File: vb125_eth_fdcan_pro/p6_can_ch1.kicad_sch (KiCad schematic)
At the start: 32 parts, among them J4 D09P33E4GL00LF, M2 B0505MT-1WR4, Q3 FDN358P, Q4 FDN358P, SW1 DS04-254-2-03BK-SMT, U8 ADM3057E

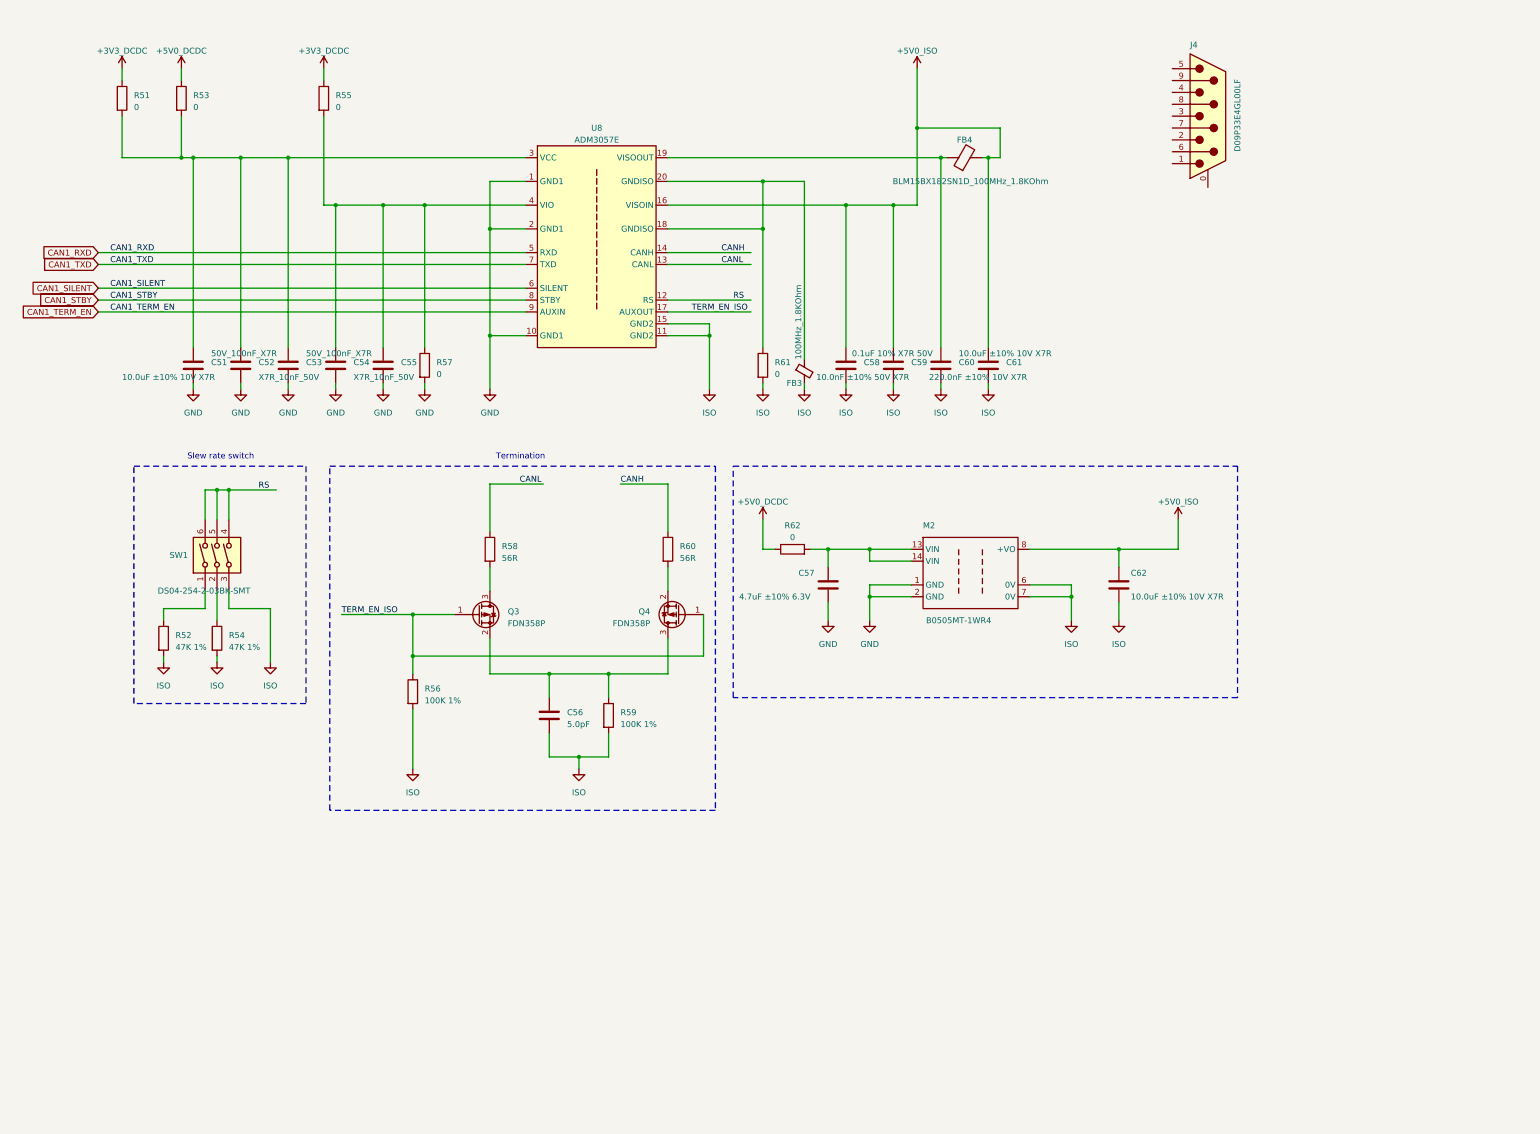
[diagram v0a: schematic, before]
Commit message: CAN schematics. Assign IO on H7.
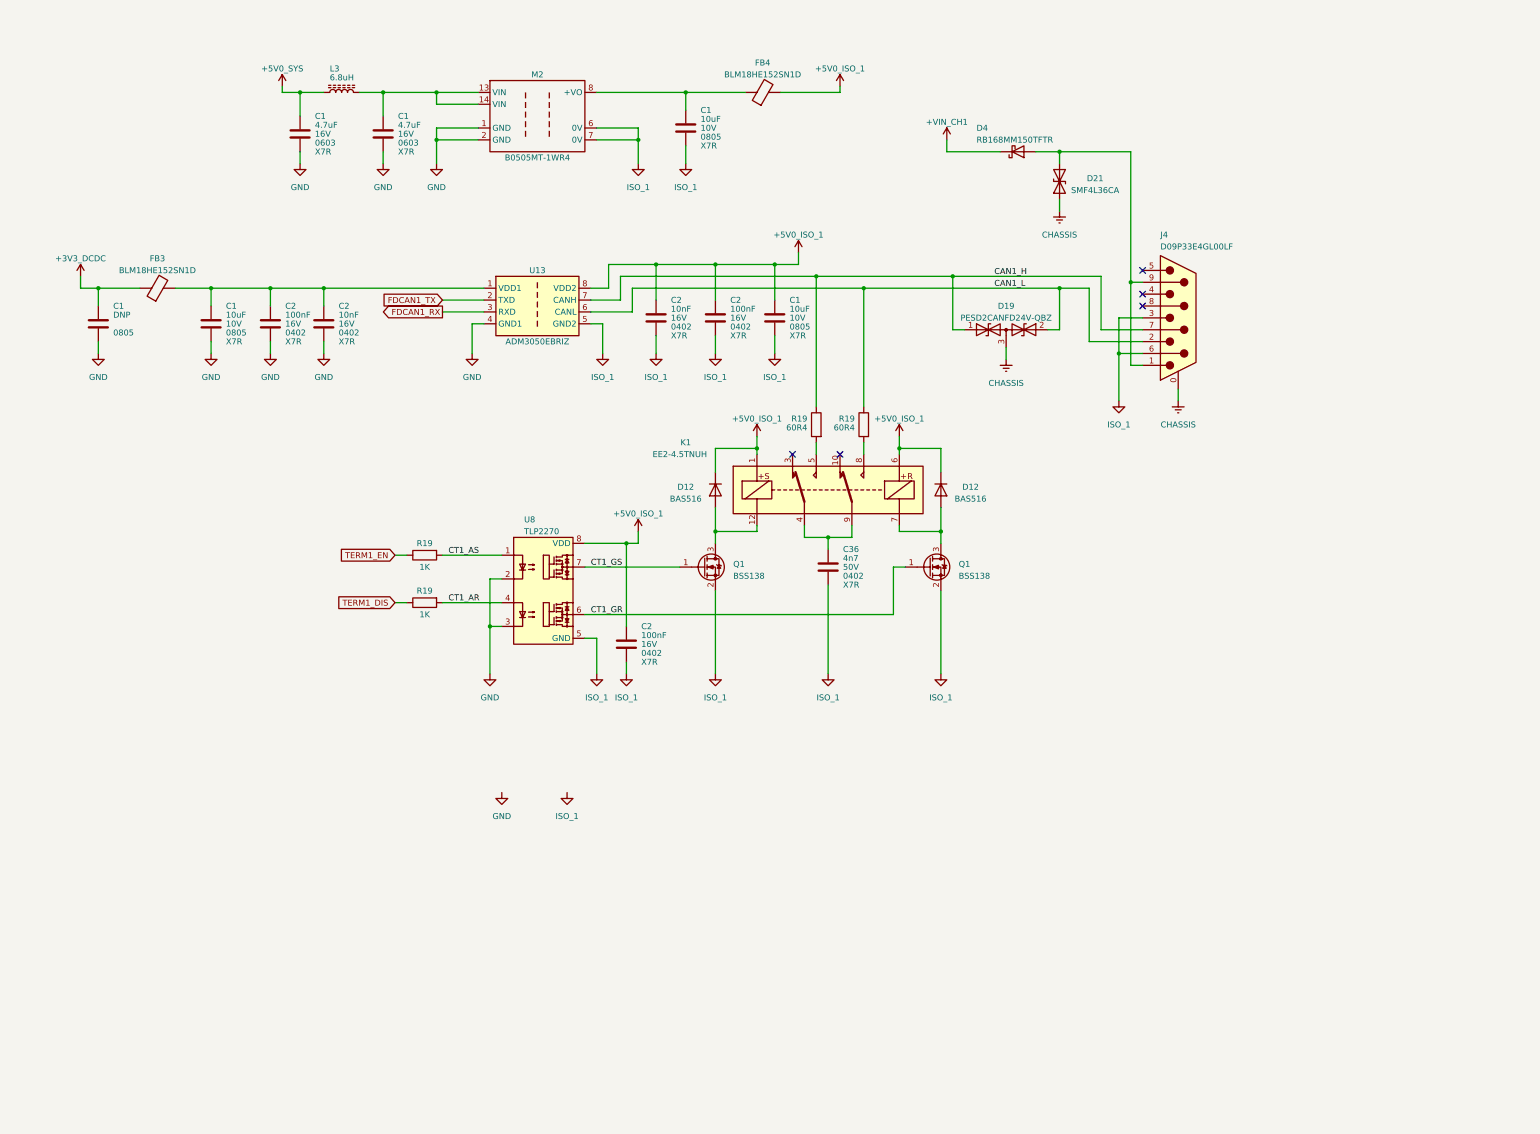
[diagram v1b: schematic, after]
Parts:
- removed C51, C61, C62: 10.0uF ±10% 10V X7R, Capacitor_SMD:C_1206_3216Metric, symbol Device:C
- removed C52, C54: 50V_100nF_X7R, Capacitor_SMD:C_0402_1005Metric, symbol Device:C
- removed C53, C55: X7R_10nF_50V, Capacitor_SMD:C_0402_1005Metric, symbol Device:C
- removed C56: 5.0pF, Capacitor_SMD:C_0402_1005Metric, symbol Device:C
- removed C57: 4.7uF ±10% 6.3V, Capacitor_SMD:C_0603_1608Metric, symbol Device:C
- removed C58: 10.0nF ±10% 50V X7R, Capacitor_SMD:C_0402_1005Metric, symbol Device:C
- removed C59: 0.1uF 10% X7R 50V, Capacitor_SMD:C_0402_1005Metric, symbol Device:C
- removed C60: 220.0nF ±10% 10V X7R, Capacitor_SMD:C_0402_1005Metric, symbol Device:C
- removed FB3: 100MHz_1.8KOhm, Resistor_SMD:R_0402_1005Metric, symbol Device:FerriteBead_Small
- removed Q3, Q4: FDN358P, Package_TO_SOT_SMD:SOT-23-3, symbol Device:Q_PMOS_GSD
- removed R51, R53, R55, R57, R61, R62: 0, Resistor_SMD:R_0402_1005Metric, symbol Device:R
- removed R52, R54: 47K 1%, Resistor_SMD:R_0402_1005Metric, symbol Device:R
- removed R56, R59: 100K 1%, Resistor_SMD:R_0402_1005Metric, symbol Device:R
- removed R58, R60: 56R, Resistor_SMD:R_0603_1608Metric, symbol Device:R
- removed SW1: DS04-254-2-03BK-SMT, Button_Switch_SMD:SW_DIP_SPSTx03_Slide_Omron_A6S-310x_W8.9mm_P2.54mm, symbol Switch:SW_DIP_x03
- removed U8: ADM3057E, Package_SO:SOIC-20W_7.5x12.8mm_P1.27mm, symbol vhrd_interface_can:ADM3057E
- added C1 (x2): 4.7uF, Capacitor_SMD:C_0603_1608Metric, symbol Device:C
- added C1 (x3): 10uF, Capacitor_SMD:C_0805_2012Metric, symbol Device:C
- added C1: DNP, Capacitor_SMD:C_0805_2012Metric, symbol Device:C
- added C2 (x3): 100nF, symbol Device:C
- added C2 (x2): 10nF, symbol Device:C
- added C36: 4n7, symbol Device:C
- added D12 (x2): BAS516, Diode_SMD:D_SOD-523, symbol Diode:BAS516
- added D19: PESD2CANFD24V-QBZ, symbol Device:D_TVS_Dual_AAC
- added D21: SMF4L36CA, symbol Device:D_TVS
- added D4: RB168MM150TFTR, Diode_SMD:D_SOD-123F, symbol Device:D_Schottky
- added FB3: BLM18HE152SN1D, Inductor_SMD:L_0603_1608Metric, symbol Device:FerriteBead
- added K1: EE2-4.5TNUH, vhrd_relay:Relay_DPDT_Kemet_EE2_NUH_DoubleCoil, symbol Relay:EE2-4.5TNUH
- added L3: 6.8uH, Inductor_SMD:L_0805_2012Metric, symbol Device:L_Ferrite
- added Q1 (x2): BSS138, Package_TO_SOT_SMD:SOT-23, symbol Transistor_FET:BSS138
- added R19 (x2): 1K, Resistor_SMD:R_0402_1005Metric, symbol Device:R
- added R19 (x2): 60R4, Resistor_SMD:R_0603_1608Metric, symbol Device:R
- added U13: ADM3050EBRIZ, vhrd_generic:RI-8-1_ADI, symbol vhrd_interface_can:ADM3050E
- added U8: TLP2270, vhrd_generic:SO8L_TOS, symbol vhrd_opto_isolators:TLP2270
- FB4: value BLM15BX182SN1D_100MHz_1.8KOhm -> BLM18HE152SN1D; footprint Resistor_SMD:R_0402_1005Metric -> Inductor_SMD:L_0603_1608Metric; DCR (none) -> 0.5Ohm; Impedance (none) -> 1.5k @ 100MHz; Irated (none) -> 500mA
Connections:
- net +5V is gone; now on an unnamed net: M2.8 (+VO)
- net ISO is gone; now on net ISO_1: M2.6 (0V), M2.7 (0V)
- net +3V3_DCDC: now also C1.1, FB3.1
- net GND: now also C1.2, C1.2, C1.2, C1.2, C2.2, C2.2, U13.4 (GND1), U8.2, U8.3
- net at M2.13 (VIN), M2.14 (VIN): now also C1.1, L3.2
- net at FB4.1: now also C1.1
- net CHASSIS: now reaches J4.0 (PAD)
- net CHASSIS: now also D19.3 (common), D21.1 (A1)
- net at J4.1: now also J4.9, D21.2 (A2), D4.2 (A)
- net CAN1_L: now reaches J4.2
- net CAN1_L: now also D19.2 (A2), R19.1, U13.6 (CANL)
- net ISO_1: now reaches J4.3
- net ISO_1: now also J4.6, C1.2, C1.2, C2.2, C2.2, C2.2, C36.2, Q1.2 (S), Q1.2 (S), U13.5 (GND2), U8.5 (GND)
- net CAN1_H: now reaches J4.7
- net CAN1_H: now also D19.1 (A1), R19.1, U13.7 (CANH)
- net +5V0_ISO renamed +5V0_ISO_1
- net +5V0_ISO_1: now also C1.1, C2.1, C2.1, C2.1, D12.1 (K), D12.1 (K), K1.1, K1.6, U13.8 (VDD2), U8.8 (VDD)
- new net: C1.1, C2.1, C2.1, FB3.2, U13.1 (VDD1)
- new net: D12.2 (A), K1.7, Q1.3 (D)
- new net: D12.2 (A), K1.12, Q1.3 (D)
- new net: C36.1, K1.4, K1.9
- new net: K1.5, R19.2
- new net: K1.8, R19.2
- new net +5V0_SYS: C1.1, L3.1
- new net +VIN_CH1: D4.1 (K)
- new net CT1_AR: R19.2, U8.4
- new net CT1_AS: R19.2, U8.1
- new net CT1_GR: Q1.1 (G), U8.6
- new net CT1_GS: Q1.1 (G), U8.7
- new net FDCAN1_RX: U13.3 (RXD)
- new net FDCAN1_TX: U13.2 (TXD)
- new net TERM1_DIS: R19.1
- new net TERM1_EN: R19.1
- no-connect marks 0 -> 5
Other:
- note removed: "Slew rate switch"
- note removed: "Termination"
- moved on the sheet: J4, M2

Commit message: Finish schematics.
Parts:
- removed D21: SMF4L36CA, symbol Device:D_TVS
- removed D4: RB168MM150TFTR, Diode_SMD:D_SOD-123F, symbol Device:D_Schottky
- added C101: Y rated, THT, Capacitor_THT:C_Disc_D7.0mm_W2.5mm_P5.00mm, symbol Device:C
- added C103: Y rated, SMD 1808, vhrd_generic:C_1808_4520Metric, symbol Device:C
- C2, C36: footprint (none) -> Capacitor_SMD:C_0402_1005Metric
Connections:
- net GND: now also C101.1, C103.1
- net +VO: now reaches C1.1, FB4.1, M2.8 (+VO)
- net +VIN_DB9: now reaches J4.1, J4.9
- net +5V0_ISO_1 renamed +5V0_ISO
- net CAN1_H renamed CAN_H
- net CAN1_L renamed CAN_L
- net CT1_AR renamed CT_AR
- net CT1_AS renamed CT_AS
- net CT1_GR renamed CT_GR
- net CT1_GS renamed CT_GS
- net FDCAN1_RX renamed FDCAN_RX
- net FDCAN1_TX renamed FDCAN_TX
- net ISO_1 renamed ISO
- net ISO: now also C101.2, C103.2
- net TERM1_DIS renamed TERM_DIS
- net TERM1_EN renamed TERM_EN

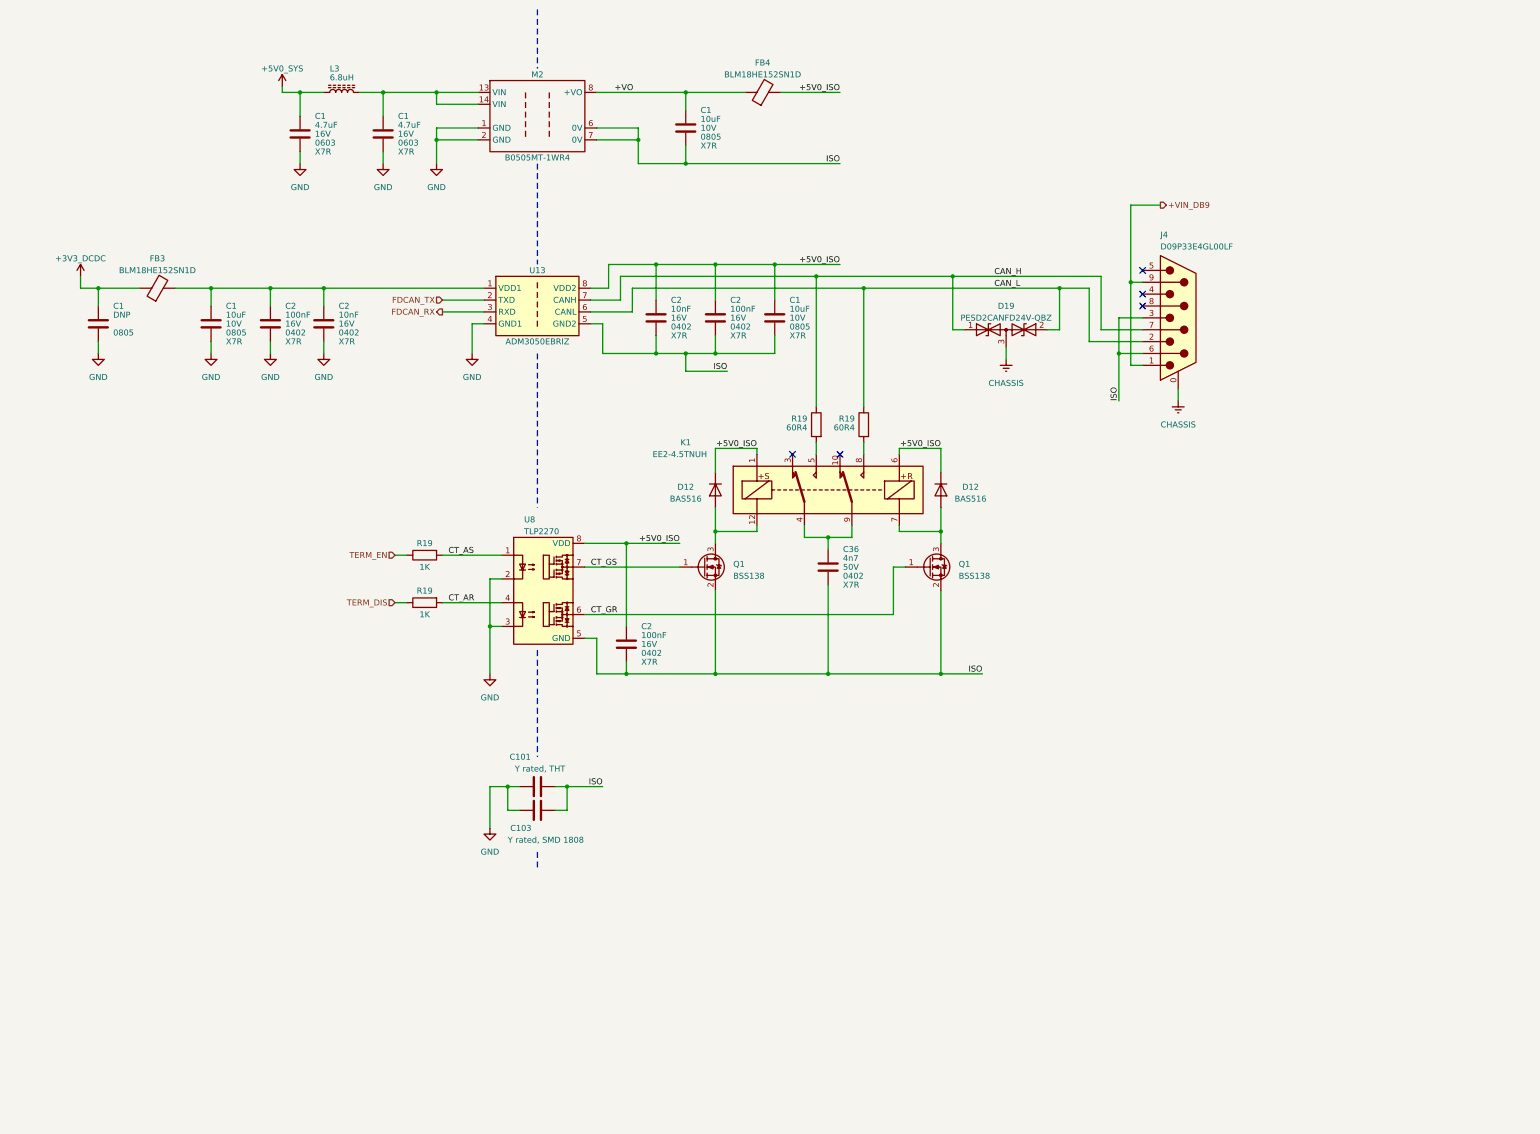
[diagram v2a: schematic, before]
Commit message: Add testpoints and set page templates.
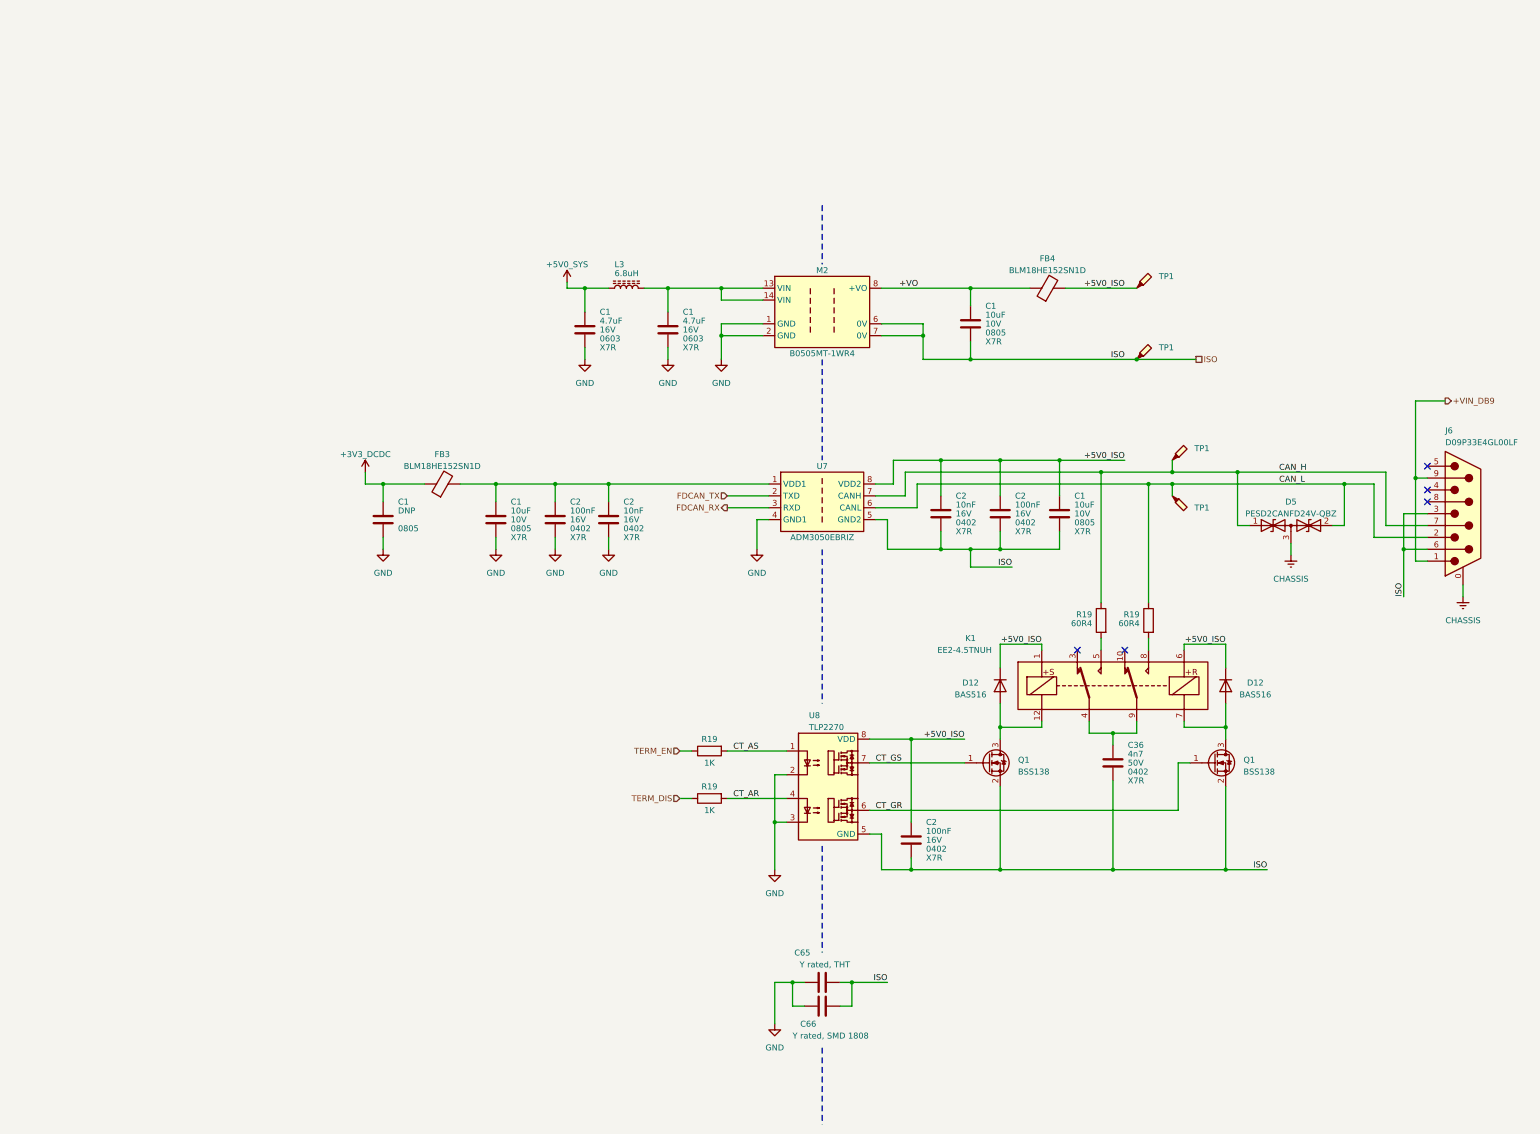
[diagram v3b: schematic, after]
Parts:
- added TP1 (x4): TestPoint_Probe, TestPoint:TestPoint_Pad_D1.5mm, symbol Connector:TestPoint_Probe
- K1: footprint vhrd_relay:Relay_DPDT_Kemet_EE2_NUH_DoubleCoil -> Relay_SMD:Relay_DPDT_Kemet_EE2_NUH_DoubleCoil
- renumbered C101 to C65, C103 to C66, D19 to D5, J4 to J6, U13 to U7
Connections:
- net +5V0_ISO: now also TP1.1
- net CAN_H: now also TP1.1
- net CAN_L: now also TP1.1
- net ISO: now also TP1.1
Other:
- company: (none) -> vhrd.tech AS
- title: (none) -> rt_bridge_pro
- moved on the sheet: C1, C2, C36, C65, C66, D12, D5, FB3, FB4, J6, K1, L3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

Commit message: Add sourcing information for resistors
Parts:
- R19: Mpn1 (none) -> RMCF0402FT1K00; Mpn2 (none) -> RC0402FR-071KL
- R19: Mpn1 (none) -> RMCF0603FT60R4; Mpn2 (none) -> CR0603-FX-60R4ELF
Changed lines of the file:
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@@
+      (effects (font (size 1.27 1.27)) hide)
+    )
+    (property "Mpn1" "RMCF0402FT1K00" (at 165.1 171.45 0)
+      (effects (font (size 1.27 1.27)) hide)
+    )
+    (property "Mpn2" "RC0402FR-071KL" (at 165.1 171.45 0)
       (effects (font (size 1.27 1.27)) hide)
     )
@@
       (effects (font (size 1.27 1.27)) hide)
     )
+    (property "Mpn1" "RMCF0603FT60R4" (at 248.92 143.51 0)
+      (effects (font (size 1.27 1.27)) hide)
+    )
+    (property "Mpn2" "CR0603-FX-60R4ELF" (at 248.92 143.51 0)
+      (effects (font (size 1.27 1.27)) hide)
+    )
     (pin "1")
     (pin "2")
@@
       (effects (font (size 1.27 1.27)) hide)
     )
+    (property "Mpn1" "RMCF0402FT1K00" (at 165.1 181.61 0)
+      (effects (font (size 1.27 1.27)) hide)
+    )
+    (property "Mpn2" "RC0402FR-071KL" (at 165.1 181.61 0)
+      (effects (font (size 1.27 1.27)) hide)
+    )
     (pin "1")
     (pin "2")
@@
       (effects (font (size 1.27 1.27)) hide)
     )
+    (property "Mpn1" "RMCF0603FT60R4" (at 259.08 143.51 0)
+      (effects (font (size 1.27 1.27)) hide)
+    )
+    (property "Mpn2" "CR0603-FX-60R4ELF" (at 259.08 143.51 0)
+      (effects (font (size 1.27 1.27)) hide)
+    )
